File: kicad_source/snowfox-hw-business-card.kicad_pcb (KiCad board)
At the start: 2 copper layers, 85 x 54 mm, 108 parts, among them CN1 Micro_SDCard, CN2 CONN_02X05, CN3 CONN_01X24, CN4 USB_OTG, CN5 CONN_01X14, CN6 CONN_01X04, Q1 SI1304BDL, Q2 BC847, SW1 TAST_VER, SW2 TAST_VER, SW3 SW_PUSH, SW4 TAST_VER, SW5 SWITCH_INV, U1 W25Q80D, U2 ATECC608A, U3 FE310-G002, U4 FT230XS, U5 TPS736XX, U6 TPS736XX, U7 M24LR, U8 BMA400, Y1 16MHz

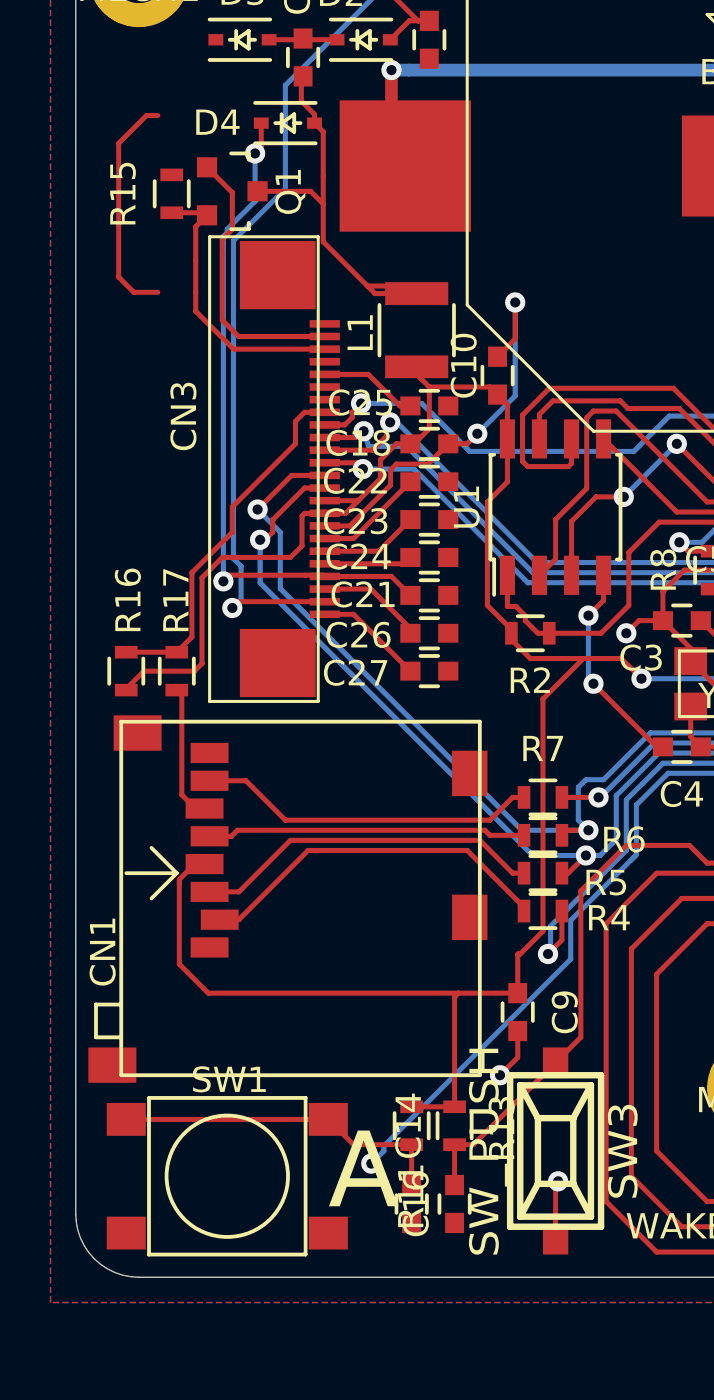
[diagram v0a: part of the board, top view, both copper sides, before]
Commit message: added some missing part numbers
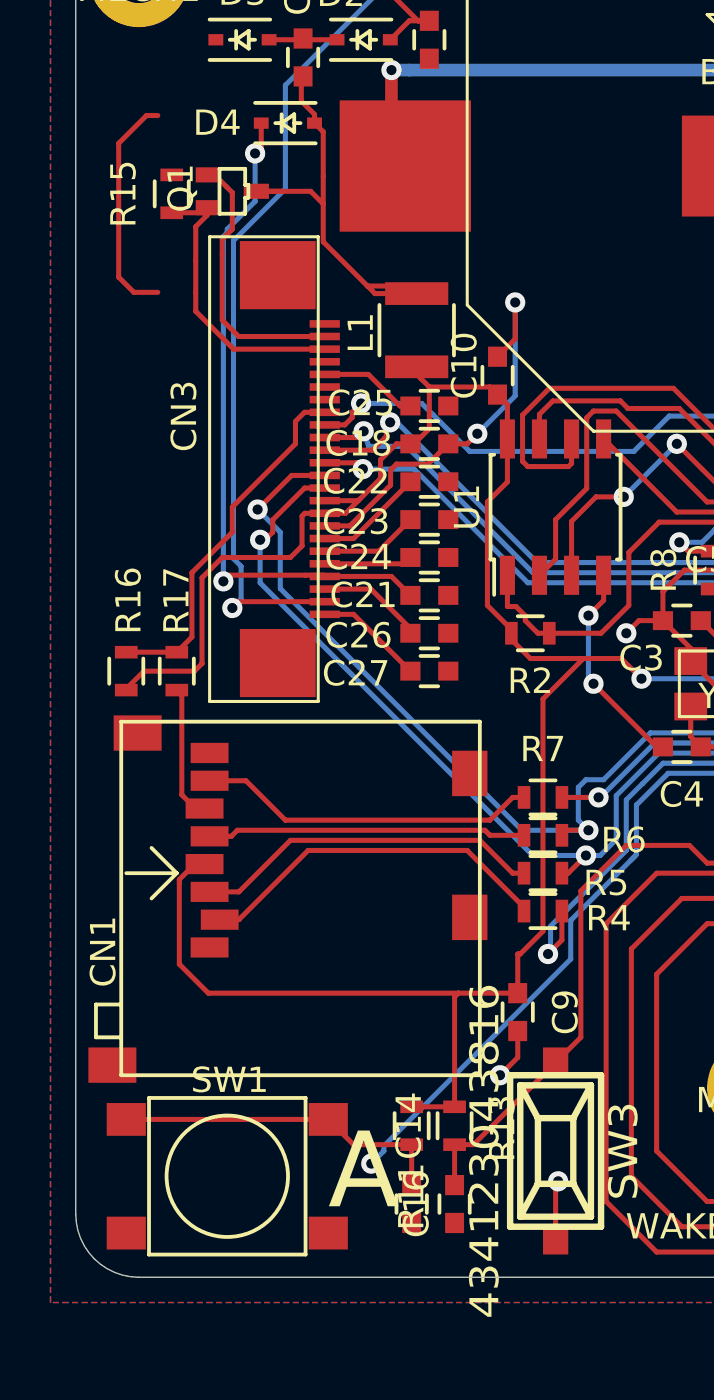
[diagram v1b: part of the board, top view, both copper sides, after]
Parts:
- C3, C4: value 15pF -> 9pF
- CN2: value CONN_02X05 -> FSH-105-04-L-DH-SL
- L1: value INDUCTOR_SMALL -> 744764147
- Q1: value SI1304BDL -> SI1308EDL; footprint SOT_TO:SOT-23 -> SOT_TO:SOT-323
- SW3: value SW_PUSH -> 434123043816
- U5: value TPS736XX -> TPS73633DBV
- U6: value TPS736XX -> TPS73618DBV
- Y1: value 16MHz -> FA-238 16.0000MB-C3
- turned Q1 to 90 degrees
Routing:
- net Net-(C20-Pad2): track 16.2 -> 17.3 mm

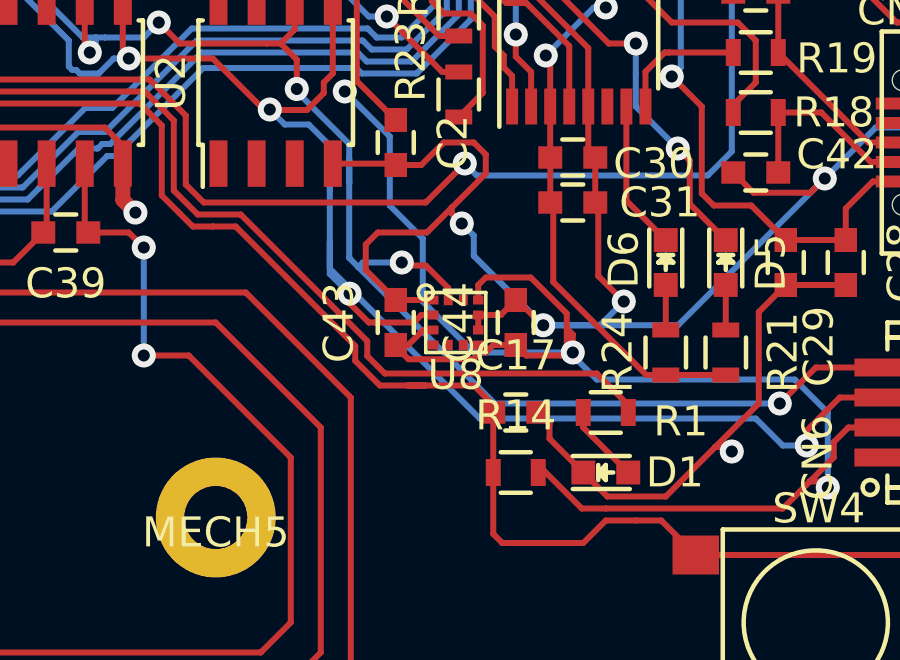
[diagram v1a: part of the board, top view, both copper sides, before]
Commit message: changed BMA400 to BMA253, changed SD-Card-Socket to MEM2061-01-188-00-A and changed battery holder to BAT-HLD-001 for cost reduction
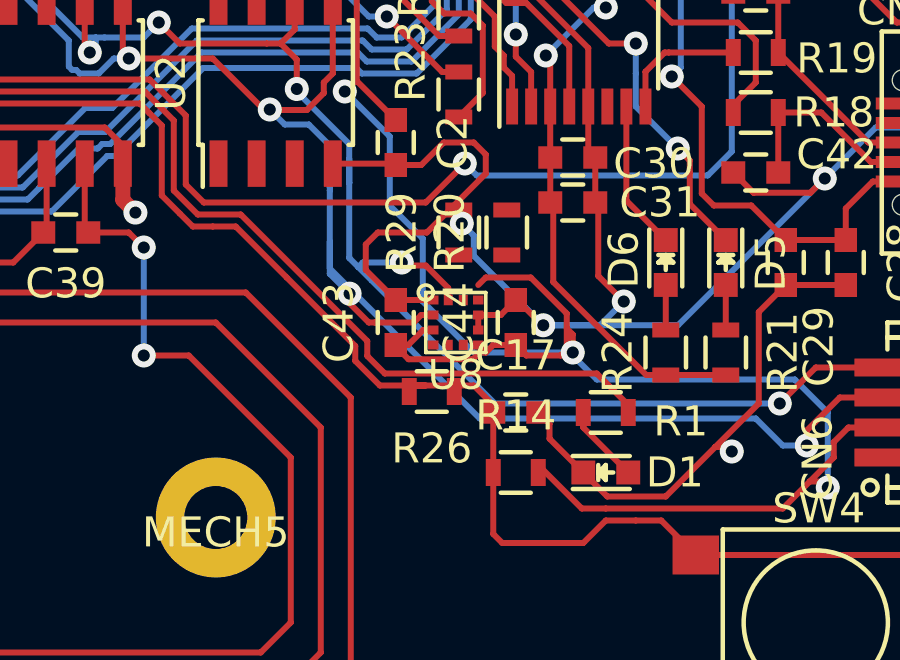
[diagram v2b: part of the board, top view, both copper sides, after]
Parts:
- added R20: DNI, resistors:R_0603, F.Cu at (145.7, 120.0)
- added R26: 0R, resistors:R_0603, F.Cu at (143.2, 125.3)
- added R29: 0R, resistors:R_0603, F.Cu at (144.1, 120.0)
- BT1, BT2: value 79523141 -> BAT-HLD-001
- CN1: value Micro_SDCard -> MEM2061-01-188-00-A
- U8: value BMA400 -> BMA253
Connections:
- U8 pad 10: +3V3 -> Net-(R20-Pad1)
- U8 pad 11: (no net) -> Net-(R29-Pad1)
- U8 pad 4: (no net) -> Net-(R26-Pad2)
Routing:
- net +3V3: track 301.9 -> 301.4 mm

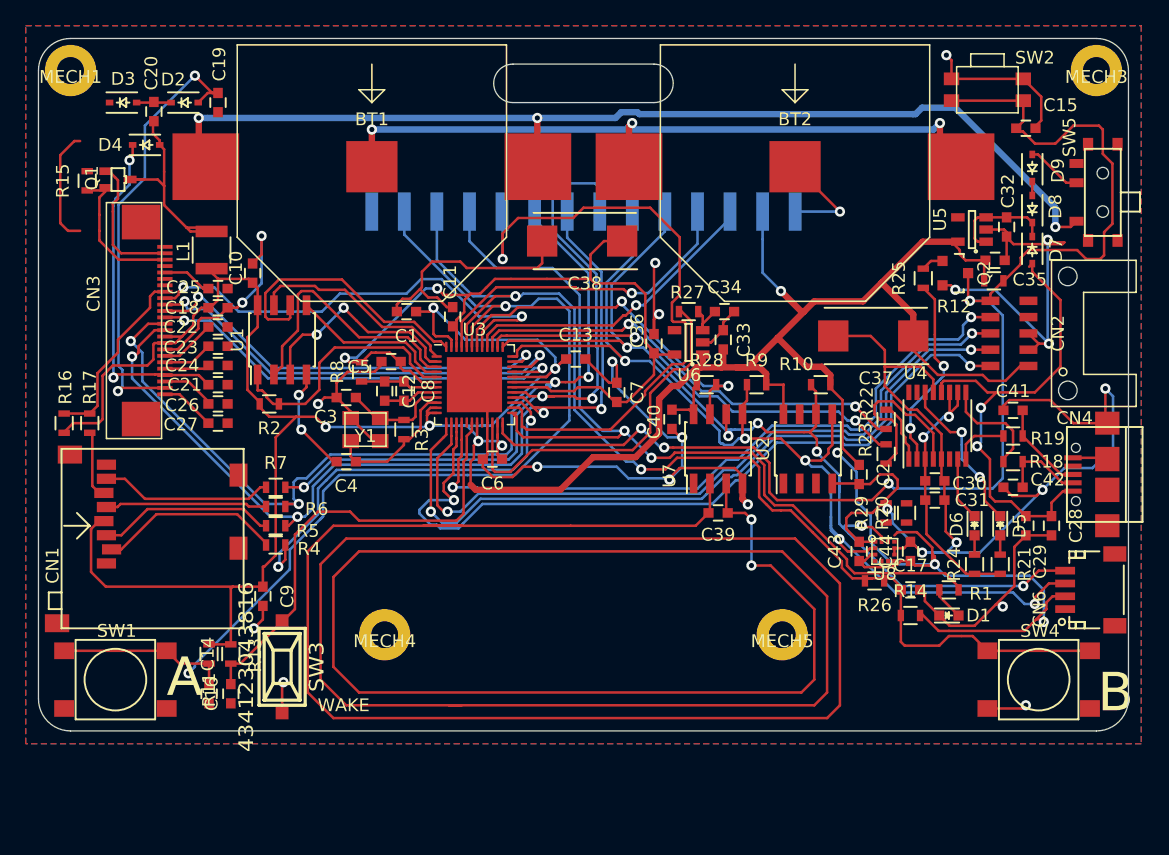
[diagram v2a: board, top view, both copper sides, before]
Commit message: optimized parts for BOM costs
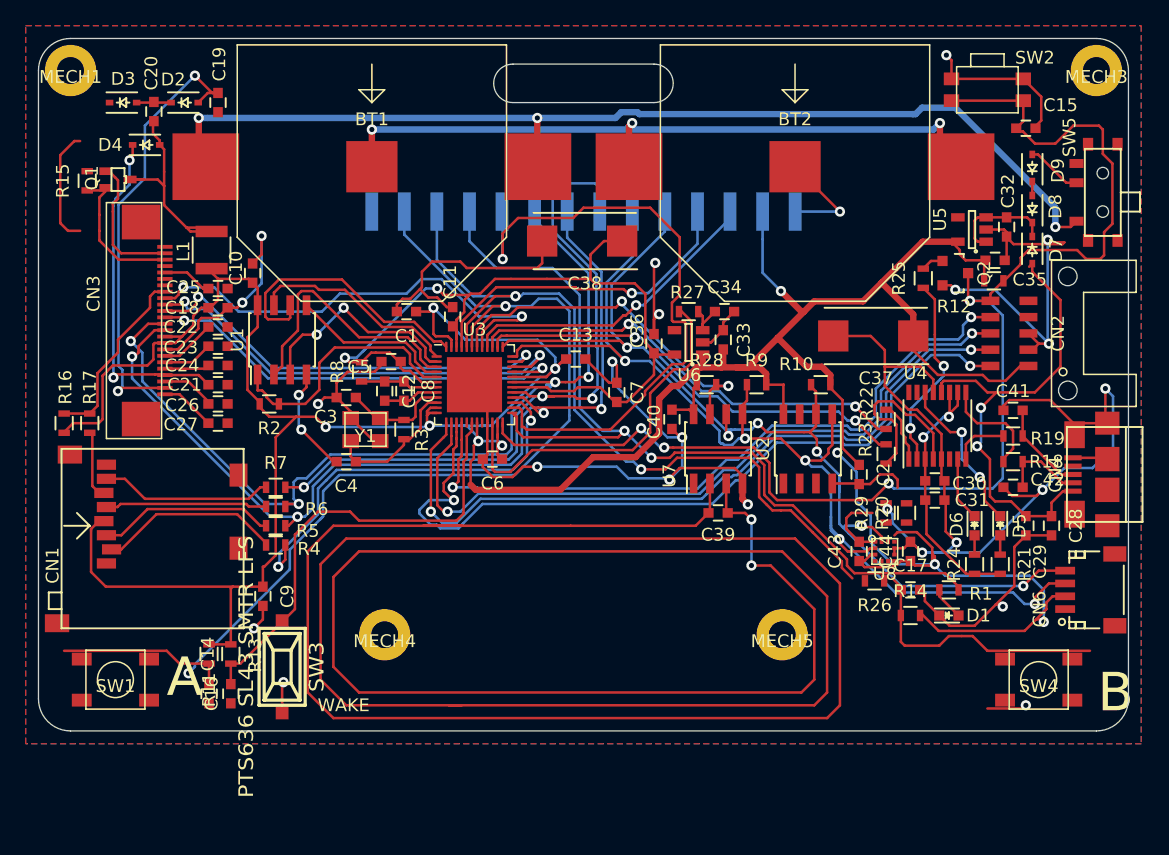
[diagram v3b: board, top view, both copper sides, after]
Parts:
- CN3: value CONN_01X24 -> SFV24R-3STBE1HLF
- CN4: value USB_OTG -> 10118192-0001LF; footprint CON_wuerth:WE_629105136821 -> CON_wuerth:10118192-000xLF
- D2, D3, D4, D7: value B0530WS -> BAT54HT1G
- D8, D9: value 1N4148WS -> BAS16HT3G
- SW1, SW4: value TAST_VER -> PTS 647 SK38 SMTR2 LFS; footprint mechanical-switches:WE_430182050816 -> mechanical-switches:CK_PTS647
- SW3: value 434123043816 -> PTS636 SL43 SMTR LFS
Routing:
- net /Microcontroller/BUTTON_B: track 84.7 -> 81.0 mm
- net GND: track 303.3 -> 299.9 mm

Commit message: connected interrupt line of BMA253, updated layout
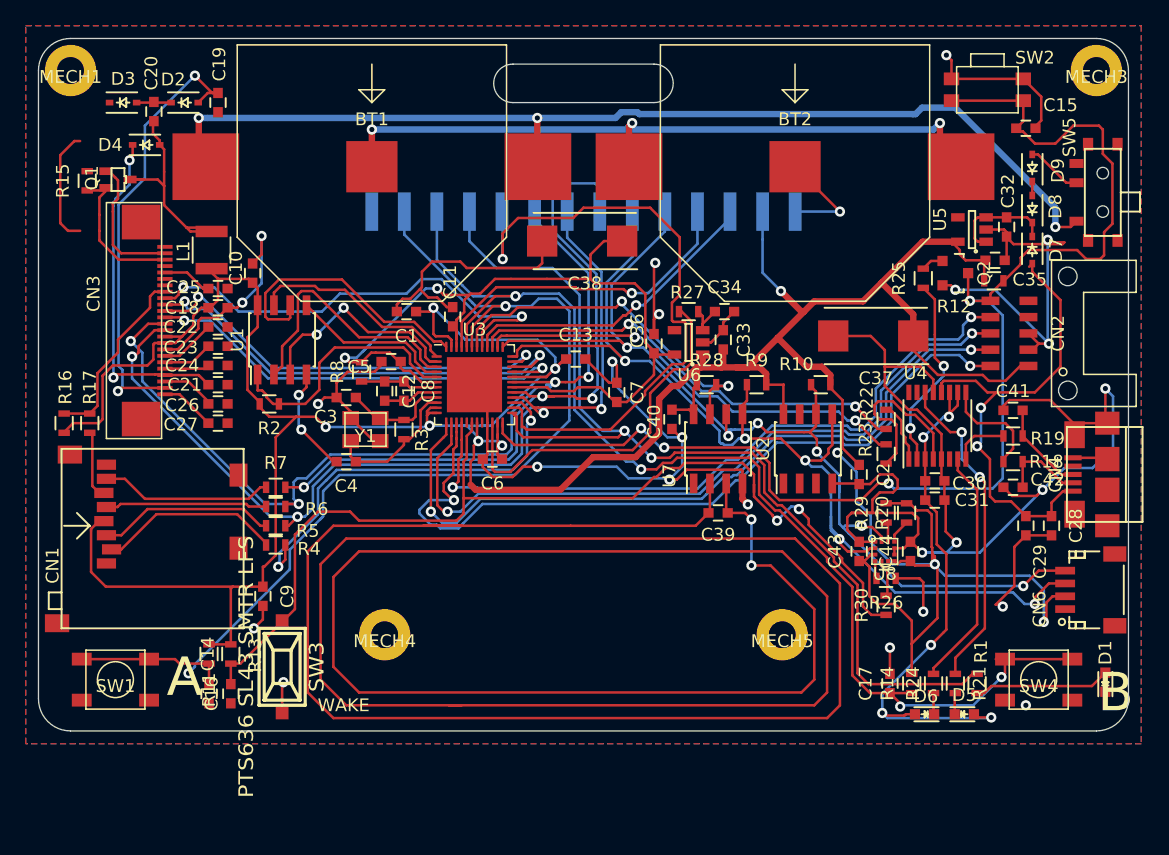
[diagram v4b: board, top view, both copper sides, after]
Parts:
- added R30: 0R, resistors:R_0603, F.Cu at (144.1, 127.2)
- moved D6 15.2 mm to (147.1, 135.7), turned to 180 degrees
- moved D5 15.0 mm to (150.2, 135.7), turned to 0 degrees
- moved D1 13.3 mm to (161.2, 133.2), turned to 90 degrees
- moved R21 9.94 mm to (149.5, 133.3)
- moved R24 9.84 mm to (147.8, 133.3)
- moved R1 7.62 mm to (151.2, 133.3), turned to 90 degrees
- moved C17 7.47 mm to (144.4, 133.3), turned to 90 degrees
- moved R14 5.30 mm to (146.1, 133.3), turned to 90 degrees
- moved R26 0.92 mm to (144.1, 125.1)
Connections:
- D5 pad 1: /USB/RX_LED -> Net-(D5-Pad1)
- D5 pad 2: Net-(D5-Pad2) -> VIO
- D6 pad 1: /USB/TX_LED -> Net-(D6-Pad1)
- D6 pad 2: Net-(D6-Pad2) -> VIO
- R21 pad 1: Net-(D5-Pad2) -> /USB/RX_LED
- R21 pad 2: VIO -> Net-(D5-Pad1)
- R24 pad 1: Net-(D6-Pad2) -> /USB/TX_LED
- R24 pad 2: VIO -> Net-(D6-Pad1)
- U8 pad 5: (no net) -> /Microcontroller/BMA_INT
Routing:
- net /Microcontroller/WAKE: track 35.9 -> 79.0 mm, vias 0 -> 2
- net VIO: track 21.5 -> 44.0 mm, vias 2 -> 5
- net /USB/TX_LED: track 4.99 -> 18.8 mm
- net /USB/RX_LED: track 12.6 -> 25.4 mm
- net /Microcontroller/BUTTON_B: track 81.0 -> 90.0 mm, vias 2 -> 4
- net /Microcontroller/LED: track 69.4 -> 77.9 mm
- net Net-(D1-Pad2): track 2.62 -> 10.7 mm
- net +3V3: track 301.4 -> 309.1 mm
- net /Microcontroller/BMA_INT: track 0.00 -> 2.93 mm
- net GND: track 299.9 -> 302.1 mm, vias 26 -> 27
- net Net-(R20-Pad1): track 0.00 -> 1.89 mm
- net Net-(D6-Pad1): track 0.00 -> 1.67 mm
- net Net-(D5-Pad1): track 0.00 -> 1.67 mm
- net /Microcontroller/BUTTON_A: track 85.4 -> 83.7 mm
- net Net-(R29-Pad1): track 0.00 -> 1.56 mm
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
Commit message: added test points, finished layout
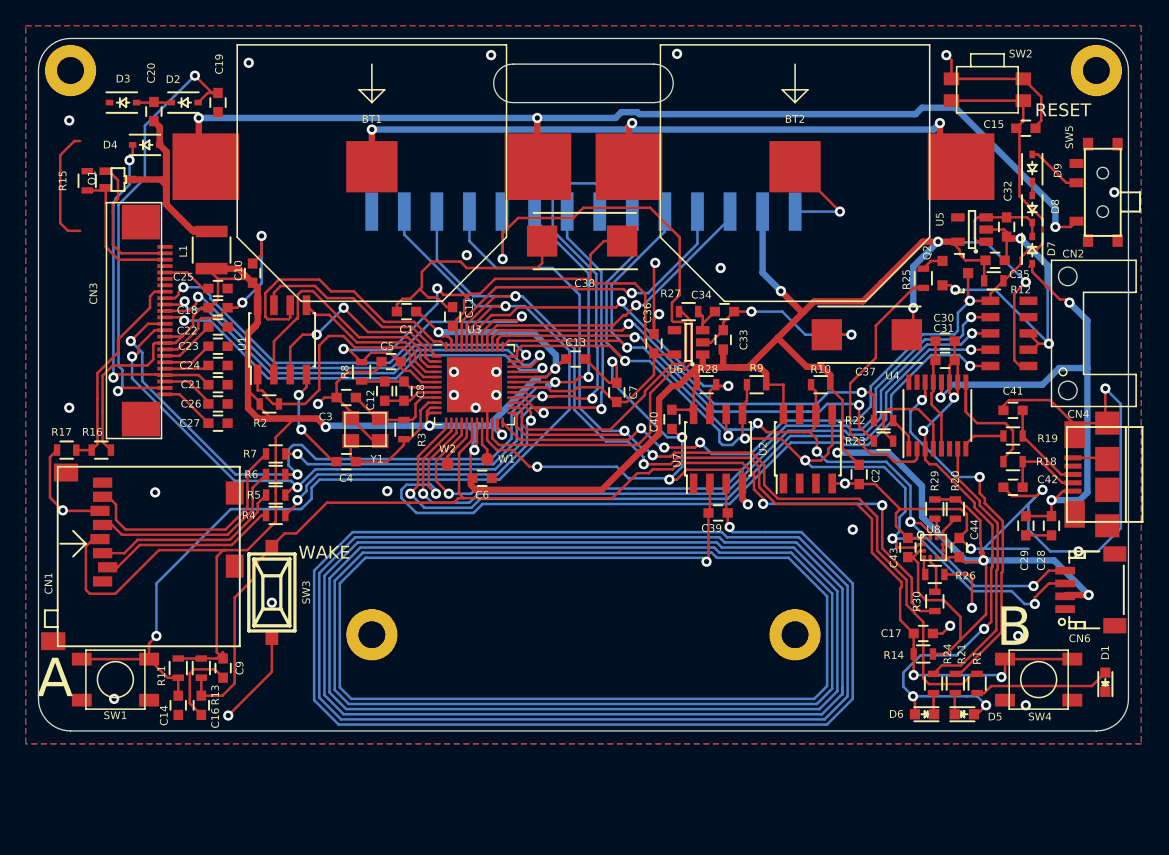
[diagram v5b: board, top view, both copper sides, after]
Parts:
- added W1: TEST_1P, wire_pads:SolderWirePad_single_1mmSMD, F.Cu at (113.0, 115.8)
- added W2: TEST_1P, wire_pads:SolderWirePad_single_1mmSMD, F.Cu at (109.9, 116.2)
- moved C30 10.9 mm to (148.7, 106.6), turned to 180 degrees
- moved C31 10.9 mm to (148.7, 108.1), turned to 180 degrees
- moved C9 6.40 mm to (92.4, 132.1)
- moved SW3 5.85 mm to (96.2, 126.2)
- moved C17 4.69 mm to (147.0, 129.4), turned to 0 degrees
- moved C43 3.81 mm to (145.8, 122.7)
- moved C44 3.81 mm to (149.8, 122.7)
- moved R20 3.81 mm to (149.5, 119.7)
- moved R26 3.81 mm to (147.9, 124.8)
- moved R29 3.81 mm to (147.9, 119.7)
- moved R30 3.81 mm to (147.9, 126.9)
- moved U8 3.81 mm to (147.8, 122.7)
- moved R16 3.58 mm to (82.9, 115.1), turned to 180 degrees
- moved R17 2.77 mm to (80.2, 115.1), turned to 180 degrees
- moved R11 2.64 mm to (88.9, 132.1)
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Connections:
- CN5 pad 1: (no net) -> GND
- U3 pad 17: (no net) -> /Microcontroller/PMU_OUT_1
- U3 pad 20: (no net) -> /Microcontroller/CLK_32K
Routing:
- net /NFC/ANTENNA: track 308.4 -> 614.5 mm
- net +3V3: track 309.1 -> 346.4 mm, vias 10 -> 13
- net RESET: track 103.7 -> 74.1 mm
- net Net-(C20-Pad2): track 17.3 -> 29.5 mm
- net /Microcontroller/WAKE: track 79.0 -> 86.0 mm
- net /Microcontroller/SPI_CS_SD: track 32.0 -> 26.0 mm
- net /USB/RTS: track 15.3 -> 21.1 mm, vias 2 -> 0
- net /Microcontroller/SPI_MISO_R: track 13.5 -> 18.6 mm
- net /USB/RX_R: track 13.9 -> 8.87 mm
- net /Microcontroller/BUTTON_B: track 90.0 -> 85.0 mm
- net VIO: track 44.0 -> 48.9 mm
- net VIN: track 38.3 -> 43.0 mm, vias 2 -> 3
- net GND: track 302.1 -> 297.6 mm, vias 27 -> 48
- net /USB/RX_LED: track 25.4 -> 29.4 mm
- net /Microcontroller/PMU_OUT_1: track 0.00 -> 3.87 mm
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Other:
- board text added: "RESET"

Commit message: exchanged rx and tx of usb serial
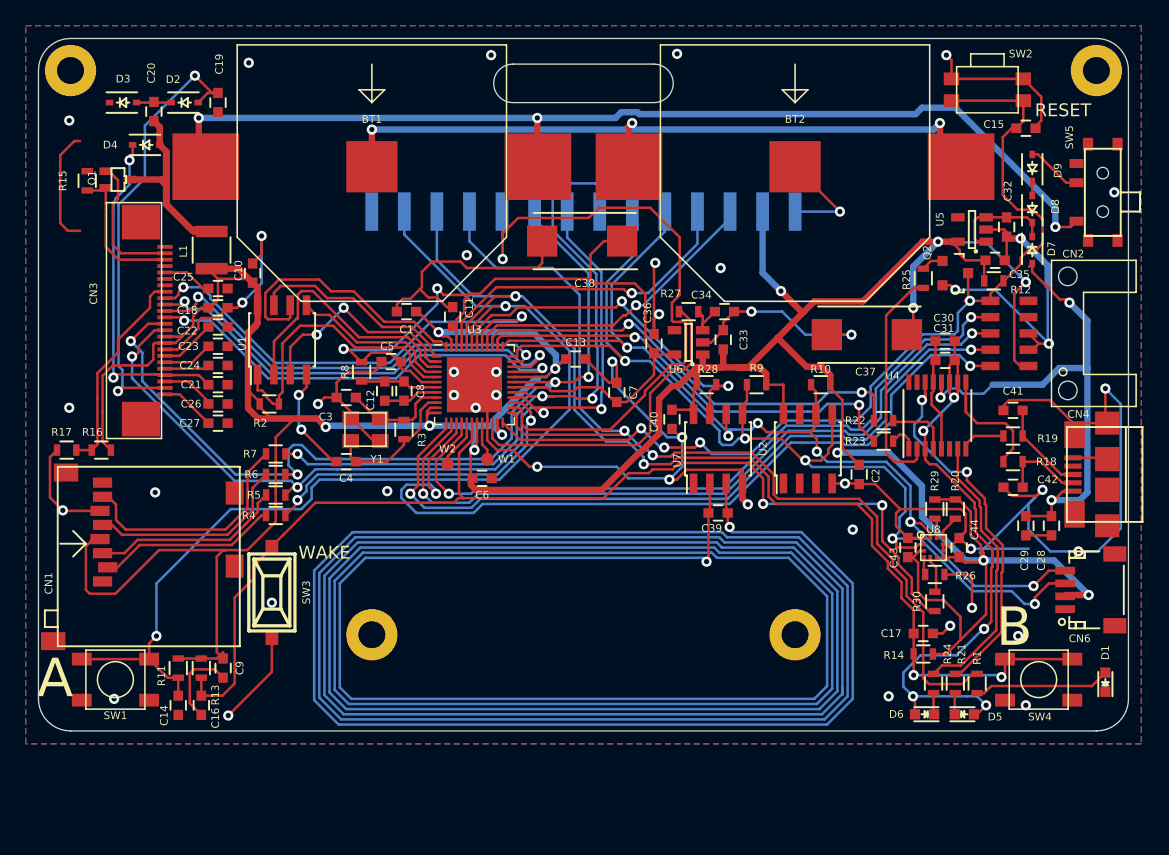
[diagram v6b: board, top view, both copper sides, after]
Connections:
- U4 pad 1: /USB/TX_R -> /USB/RX_R
- U4 pad 4: /USB/RX_R -> /USB/TX_R
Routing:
- net /USB/RX_R: track 8.87 -> 2.31 mm
- net /USB/RTS: track 21.1 -> 18.1 mm
- net /USB/TX_R: track 2.71 -> 5.01 mm
- net RESET: track 74.1 -> 75.9 mm
- net /Microcontroller/QSPI_CS: track 21.7 -> 23.0 mm
- net /USB/RX_LED: track 29.4 -> 28.8 mm
- net GND: track 297.6 -> 297.5 mm, vias 48 -> 49
